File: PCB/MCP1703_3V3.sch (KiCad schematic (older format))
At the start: 3 parts

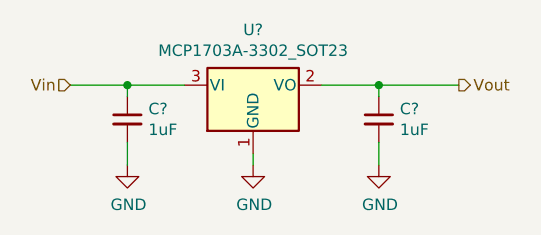
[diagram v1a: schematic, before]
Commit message: Added IEC connector and organised
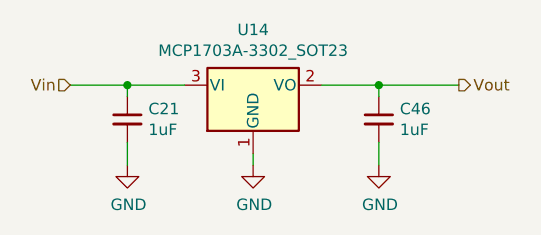
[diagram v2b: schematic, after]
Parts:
- gave numbers to parts that had none: 3
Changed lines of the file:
@@
 P 5900 3850
 AR Path="/5E880E11/5E942F93" Ref="U?"  Part="1"
-AR Path="/5E880E11/5E940C9C/5E942F93" Ref="U?"  Part="1"
-F 0 "U?" H 5900 4092 50  0000 C CNN
+AR Path="/5E880E11/5E940C9C/5E942F93" Ref="U14"  Part="1"
+F 0 "U14" H 5900 4092 50  0000 C CNN
 F 1 "MCP1703A-3302_SOT23" H 5900 4001 50  0000 C CNN
 F 2 "Package_TO_SOT_SMD:SOT-23" H 5900 4050 50  0001 C CNN
@@
 Vout
 $Comp
-L Device:C_Small C?
+L Device:C_Small C21
 U 1 1 5E944295
 P 5350 4000
-F 0 "C?" H 5442 4046 50  0000 L CNN
+F 0 "C21" H 5442 4046 50  0000 L CNN
 F 1 "1uF" H 5442 3955 50  0000 L CNN
 F 2 "" H 5350 4000 50  0001 C CNN
@@
 $EndComp
 $Comp
-L Device:C_Small C?
+L Device:C_Small C46
 U 1 1 5E944511
 P 6450 4000
-F 0 "C?" H 6542 4046 50  0000 L CNN
+F 0 "C46" H 6542 4046 50  0000 L CNN
 F 1 "1uF" H 6542 3955 50  0000 L CNN
 F 2 "" H 6450 4000 50  0001 C CNN
@@
 	6450 3850 6800 3850
 $Comp
-L power:GND #PWR?
+L power:GND #PWR065
 U 1 1 5E944E6F
 P 5350 4200
-F 0 "#PWR?" H 5350 3950 50  0001 C CNN
+F 0 "#PWR065" H 5350 3950 50  0001 C CNN
 F 1 "GND" H 5355 4027 50  0000 C CNN
 F 2 "" H 5350 4200 50  0001 C CNN
@@
 	5350 4200 5350 4100
 $Comp
-L power:GND #PWR?
+L power:GND #PWR0138
 U 1 1 5E945281
 P 5900 4200
-F 0 "#PWR?" H 5900 3950 50  0001 C CNN
+F 0 "#PWR0138" H 5900 3950 50  0001 C CNN
 F 1 "GND" H 5905 4027 50  0000 C CNN
 F 2 "" H 5900 4200 50  0001 C CNN
@@
 $EndComp
 $Comp
-L power:GND #PWR?
+L power:GND #PWR0139
 U 1 1 5E9453D3
 P 6450 4200
-F 0 "#PWR?" H 6450 3950 50  0001 C CNN
+F 0 "#PWR0139" H 6450 3950 50  0001 C CNN
 F 1 "GND" H 6455 4027 50  0000 C CNN
 F 2 "" H 6450 4200 50  0001 C CNN

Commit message: Checkpoint
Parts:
- C21, C46: Dielectric (none) -> X7R; Voltage Rating (none) -> 6.3V
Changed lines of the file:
@@
 $Descr A4 11693 8268
 encoding utf-8
-Sheet 14 22
+Sheet 13 22
 Title ""
 Date ""
@@
 F 2 "" H 5350 4000 50  0001 C CNN
 F 3 "~" H 5350 4000 50  0001 C CNN
+F 4 "X7R" H 5350 4000 50  0001 C CNN "Dielectric"
+F 5 "6.3V" H 5350 4000 50  0001 C CNN "Voltage Rating"
 	1    5350 4000
 	1    0    0    -1
@@
 F 2 "" H 6450 4000 50  0001 C CNN
 F 3 "~" H 6450 4000 50  0001 C CNN
+F 4 "X7R" H 6450 4000 50  0001 C CNN "Dielectric"
+F 5 "6.3V" H 6450 4000 50  0001 C CNN "Voltage Rating"
 	1    6450 4000
 	1    0    0    -1

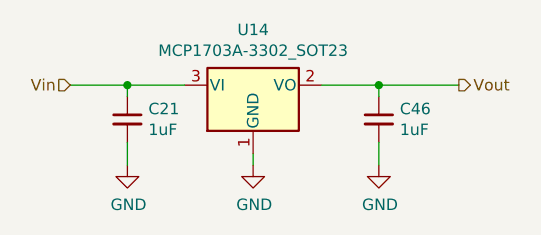
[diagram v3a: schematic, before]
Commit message: Added remaining test points
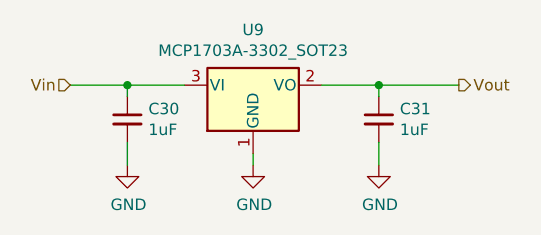
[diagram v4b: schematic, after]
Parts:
- renumbered C21 to C30, C46 to C31, U14 to U9
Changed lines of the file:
@@
 P 5900 3850
 AR Path="/5E880E11/5E942F93" Ref="U?"  Part="1"
-AR Path="/5E880E11/5E940C9C/5E942F93" Ref="U14"  Part="1"
-F 0 "U14" H 5900 4092 50  0000 C CNN
+AR Path="/5E880E11/5E940C9C/5E942F93" Ref="U9"  Part="1"
+F 0 "U9" H 5900 4092 50  0000 C CNN
 F 1 "MCP1703A-3302_SOT23" H 5900 4001 50  0000 C CNN
 F 2 "Package_TO_SOT_SMD:SOT-23" H 5900 4050 50  0001 C CNN
@@
 Vout
 $Comp
-L Device:C_Small C21
+L Device:C_Small C30
 U 1 1 5E944295
 P 5350 4000
-F 0 "C21" H 5442 4046 50  0000 L CNN
+F 0 "C30" H 5442 4046 50  0000 L CNN
 F 1 "1uF" H 5442 3955 50  0000 L CNN
 F 2 "" H 5350 4000 50  0001 C CNN
@@
 $EndComp
 $Comp
-L Device:C_Small C46
+L Device:C_Small C31
 U 1 1 5E944511
 P 6450 4000
-F 0 "C46" H 6542 4046 50  0000 L CNN
+F 0 "C31" H 6542 4046 50  0000 L CNN
 F 1 "1uF" H 6542 3955 50  0000 L CNN
 F 2 "" H 6450 4000 50  0001 C CNN
@@
 	6450 3850 6800 3850
 $Comp
-L power:GND #PWR065
+L power:GND #PWR087
 U 1 1 5E944E6F
 P 5350 4200
-F 0 "#PWR065" H 5350 3950 50  0001 C CNN
+F 0 "#PWR087" H 5350 3950 50  0001 C CNN
 F 1 "GND" H 5355 4027 50  0000 C CNN
 F 2 "" H 5350 4200 50  0001 C CNN
@@
 	5350 4200 5350 4100
 $Comp
-L power:GND #PWR0138
+L power:GND #PWR088
 U 1 1 5E945281
 P 5900 4200
-F 0 "#PWR0138" H 5900 3950 50  0001 C CNN
+F 0 "#PWR088" H 5900 3950 50  0001 C CNN
 F 1 "GND" H 5905 4027 50  0000 C CNN
 F 2 "" H 5900 4200 50  0001 C CNN
@@
 $EndComp
 $Comp
-L power:GND #PWR0139
+L power:GND #PWR089
 U 1 1 5E9453D3
 P 6450 4200
-F 0 "#PWR0139" H 6450 3950 50  0001 C CNN
+F 0 "#PWR089" H 6450 3950 50  0001 C CNN
 F 1 "GND" H 6455 4027 50  0000 C CNN
 F 2 "" H 6450 4200 50  0001 C CNN

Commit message: Added majority footprints
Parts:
- C30, C31: footprint (none) -> Capacitor_SMD:C_0603_1608Metric
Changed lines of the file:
@@
 F 0 "C30" H 5442 4046 50  0000 L CNN
 F 1 "1uF" H 5442 3955 50  0000 L CNN
-F 2 "" H 5350 4000 50  0001 C CNN
+F 2 "Capacitor_SMD:C_0603_1608Metric" H 5350 4000 50  0001 C CNN
 F 3 "~" H 5350 4000 50  0001 C CNN
 F 4 "X7R" H 5350 4000 50  0001 C CNN "Dielectric"
@@
 F 0 "C31" H 6542 4046 50  0000 L CNN
 F 1 "1uF" H 6542 3955 50  0000 L CNN
-F 2 "" H 6450 4000 50  0001 C CNN
+F 2 "Capacitor_SMD:C_0603_1608Metric" H 6450 4000 50  0001 C CNN
 F 3 "~" H 6450 4000 50  0001 C CNN
 F 4 "X7R" H 6450 4000 50  0001 C CNN "Dielectric"
